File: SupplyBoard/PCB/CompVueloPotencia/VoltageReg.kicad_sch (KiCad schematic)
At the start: 4 parts

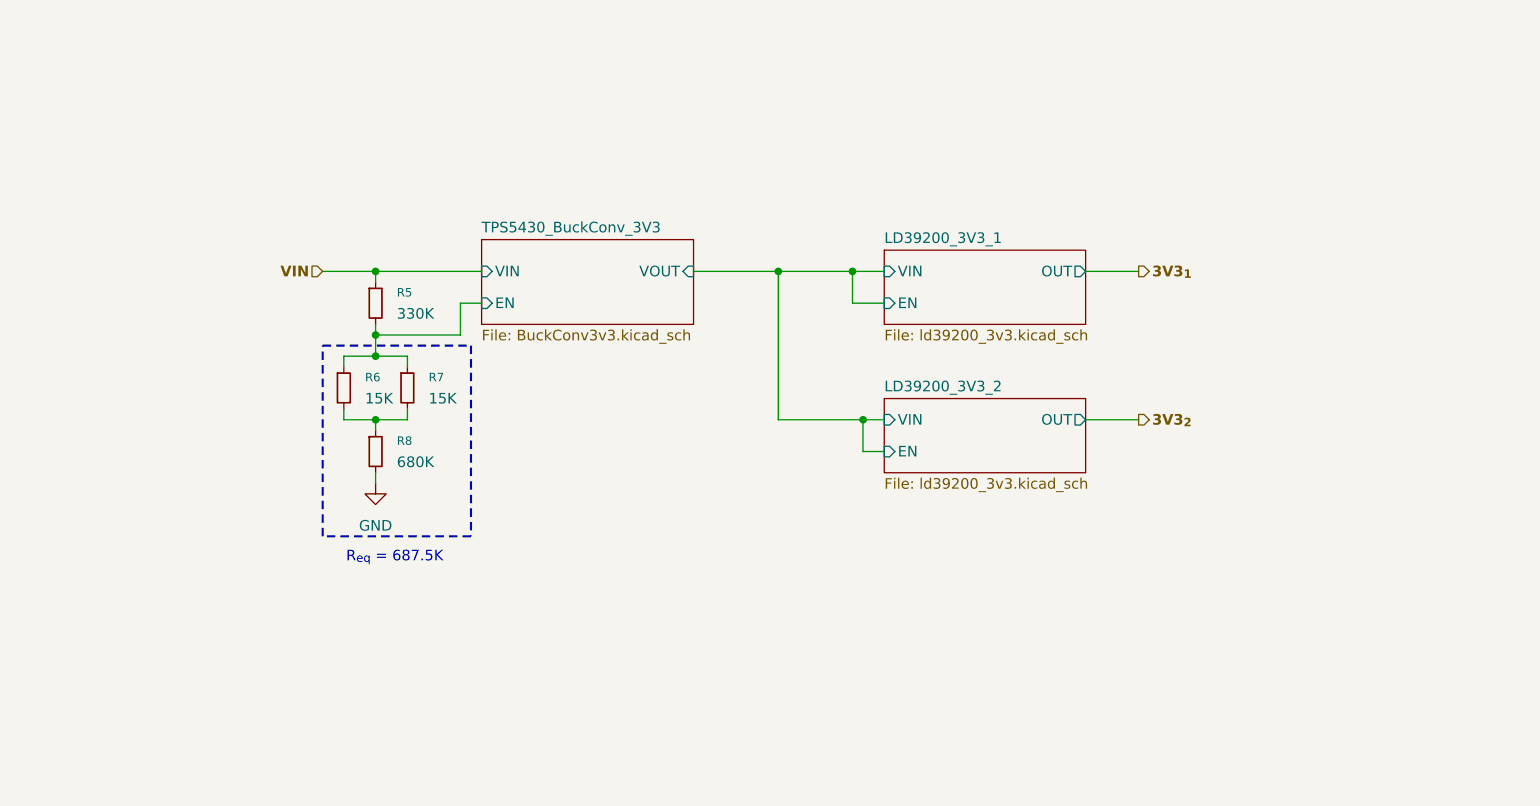
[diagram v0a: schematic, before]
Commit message: SupplyBoard - finish current sense
Finish the Current Sensor Circuit and add more 3.3V out, i change de microcontroles to a mcu that have the exact GPIO's
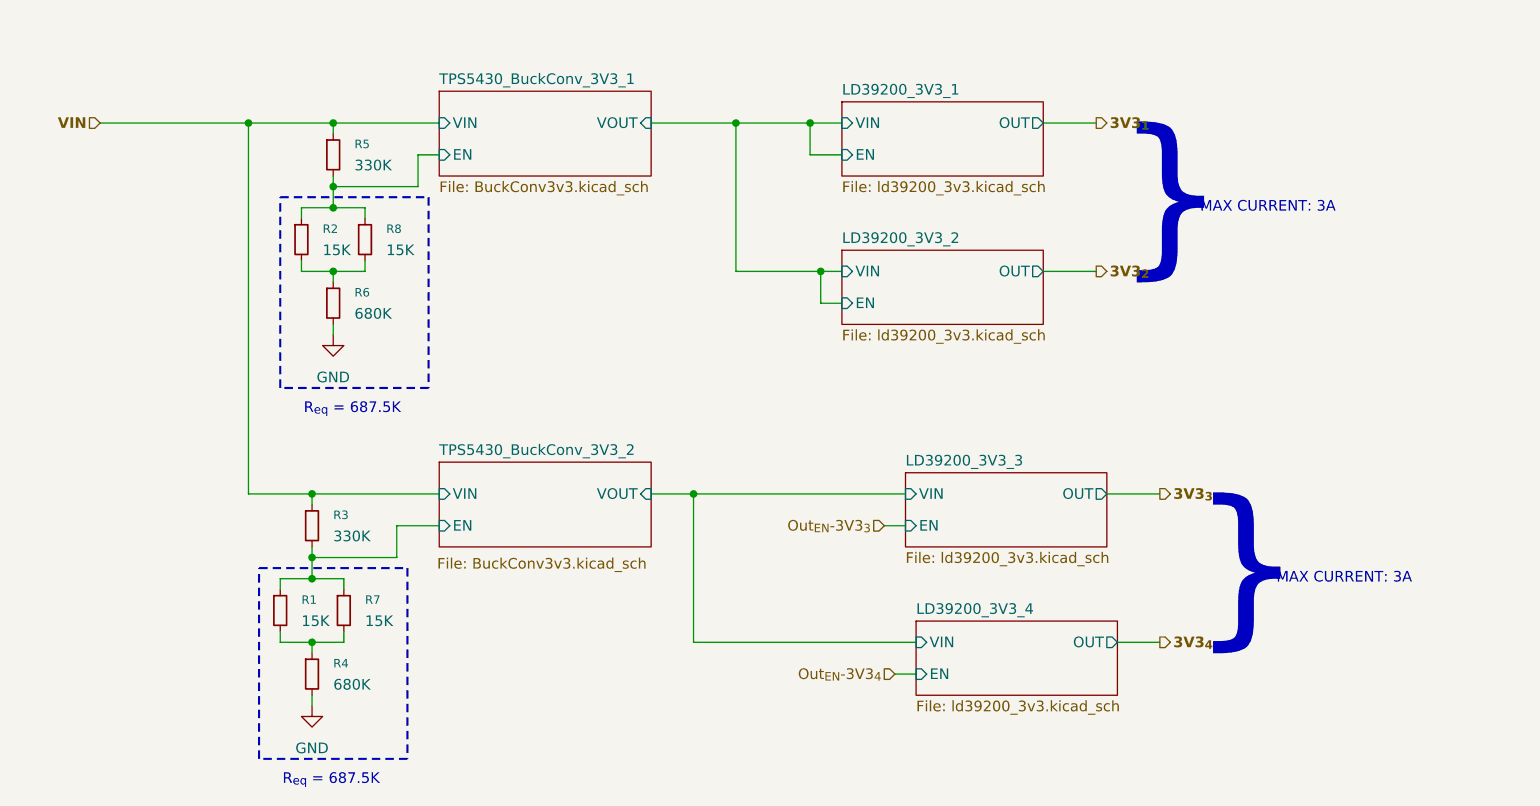
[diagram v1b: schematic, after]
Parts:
- added R1, R7: 15K, symbol Device:R_Small
- added R3: 330K, symbol Device:R_Small
- added R4: 680K, symbol Device:R_Small
- renumbered R6 to R2, R8 to R6, R7 to R8
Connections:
- net GND: now also R4.2
- net VIN: now also R3.1
- new net: R1.2, R4.1, R7.2
- new net TPS5430_BuckConv_3V3_2/EN: R1.1, R3.2, R7.1
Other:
- sheet TPS5430_BuckConv_3V3 renamed TPS5430_BuckConv_3V3_1
- added sheet LD39200_3V3_3 (ld39200_3v3.kicad_sch)
- added sheet LD39200_3V3_4 (ld39200_3v3.kicad_sch)
- added sheet TPS5430_BuckConv_3V3_2 (BuckConv3v3.kicad_sch)
- note added: "MAX CURRENT: 3A"
- note added: "}"
- moved on the sheet: R2, R5, R6, R8

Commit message: SupplyBoard - update layout
schematic completed and PCB layout started; only the routing of the traces remains to be done
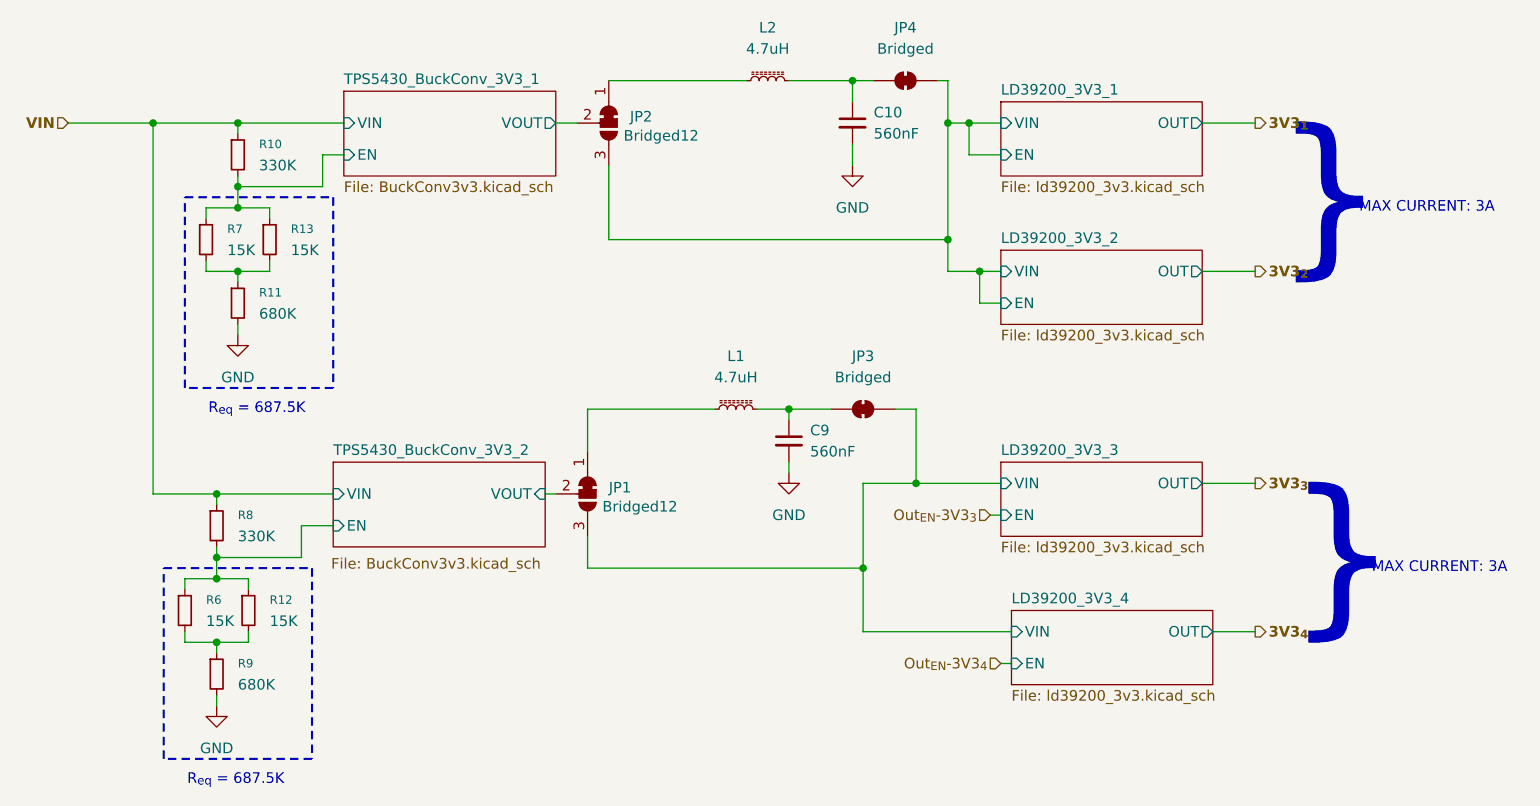
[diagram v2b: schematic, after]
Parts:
- added C10, C9: 560nF, Capacitor_SMD:C_0805_2012Metric_Pad1.18x1.45mm_HandSolder, symbol Device:C_Small
- added JP1, JP2: Bridged12, Jumper:SolderJumper-3_P1.3mm_Bridged12_RoundedPad1.0x1.5mm, symbol Jumper:SolderJumper_3_Bridged12
- added JP3, JP4: Bridged, Jumper:SolderJumper-2_P1.3mm_Bridged_RoundedPad1.0x1.5mm, symbol Jumper:SolderJumper_2_Bridged
- added L1, L2: 4.7uH, Inductor_SMD:L_Bourns_SRN6045TA, symbol Device:L_Ferrite_Small
- R10: renamed from R5; footprint (none) -> Resistor_SMD:R_0805_2012Metric_Pad1.20x1.40mm_HandSolder
- R11: renamed from R6; footprint (none) -> Resistor_SMD:R_0805_2012Metric_Pad1.20x1.40mm_HandSolder
- R12: renamed from R7; footprint (none) -> Resistor_SMD:R_0805_2012Metric_Pad1.20x1.40mm_HandSolder
- R13: renamed from R8; footprint (none) -> Resistor_SMD:R_0805_2012Metric_Pad1.20x1.40mm_HandSolder
- R6: renamed from R1; footprint (none) -> Resistor_SMD:R_0805_2012Metric_Pad1.20x1.40mm_HandSolder
- R7: renamed from R2; footprint (none) -> Resistor_SMD:R_0805_2012Metric_Pad1.20x1.40mm_HandSolder
- R8: renamed from R3; footprint (none) -> Resistor_SMD:R_0805_2012Metric_Pad1.20x1.40mm_HandSolder
- R9: renamed from R4; footprint (none) -> Resistor_SMD:R_0805_2012Metric_Pad1.20x1.40mm_HandSolder
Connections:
- net GND: now also C10.2, C9.2
- net LD39200_3V3_1/EN: now also JP2.3 (B), JP4.2 (B)
- net LD39200_3V3_3/VIN: now also JP1.3 (B), JP3.2 (B)
- new net: JP2.1 (A), L2.1
- new net: C10.1, JP4.1 (A), L2.2
- new net: C9.1, JP3.1 (A), L1.2
- new net: JP1.1 (A), L1.1
- new net TPS5430_BuckConv_3V3_1/VOUT: JP2.2 (C)
- new net TPS5430_BuckConv_3V3_2/VOUT: JP1.2 (C)
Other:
- moved on the sheet: R10, R11, R12, R13, R6, R7, R8, R9
